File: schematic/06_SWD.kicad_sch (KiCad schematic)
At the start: 8 parts, among them J8 SWD_10pin, SW2 RESET

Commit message: Exclude JP1, JP2, TP1-TP20 from BOM (attrs only, sch+pcb)
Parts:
- TP10, TP7, TP8, TP9: now left out of the parts list
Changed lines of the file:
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@@
 		(unit 1)
 		(exclude_from_sim no)
-		(in_bom yes)
+		(in_bom no)
 		(on_board yes)
 		(dnp no)
@@
 		(unit 1)
 		(exclude_from_sim no)
-		(in_bom yes)
+		(in_bom no)
 		(on_board yes)
 		(dnp no)
@@
 		(unit 1)
 		(exclude_from_sim no)
-		(in_bom yes)
+		(in_bom no)
 		(on_board yes)
 		(dnp no)
@@
 		(unit 1)
 		(exclude_from_sim no)
-		(in_bom yes)
-		(on_board yes)
-		(dnp no)
+		(in_bom no)
+		(on_board yes)
+		(dnp no)

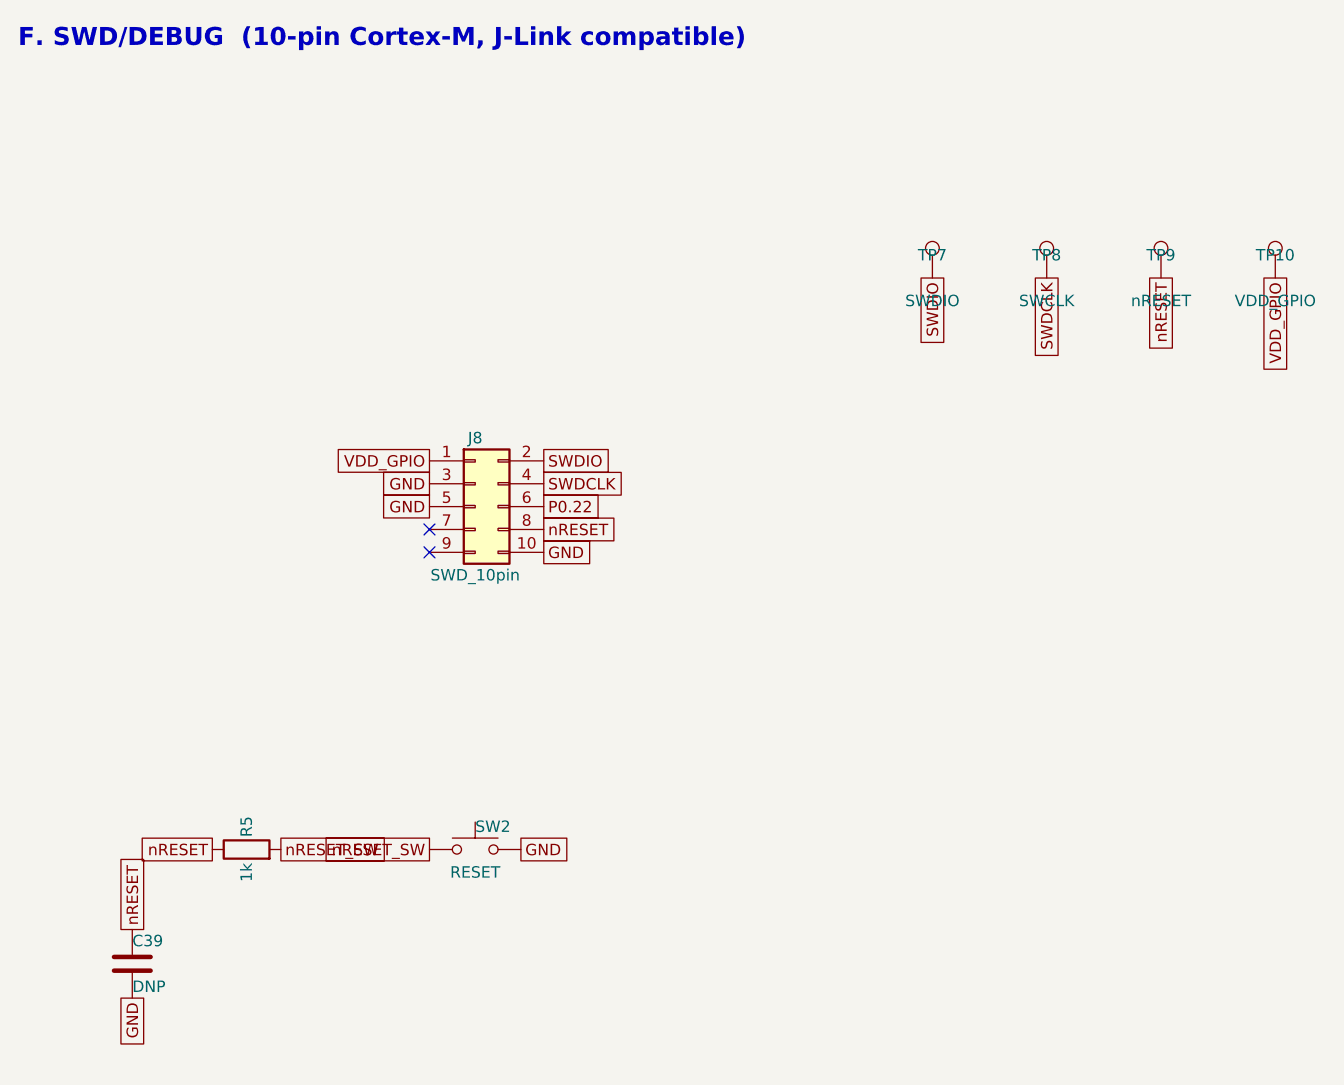
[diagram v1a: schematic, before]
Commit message: v2: simplify to UART modem module (J20 host header, LXC translators); remove J1, J3, J6, J9-J18, optional parts
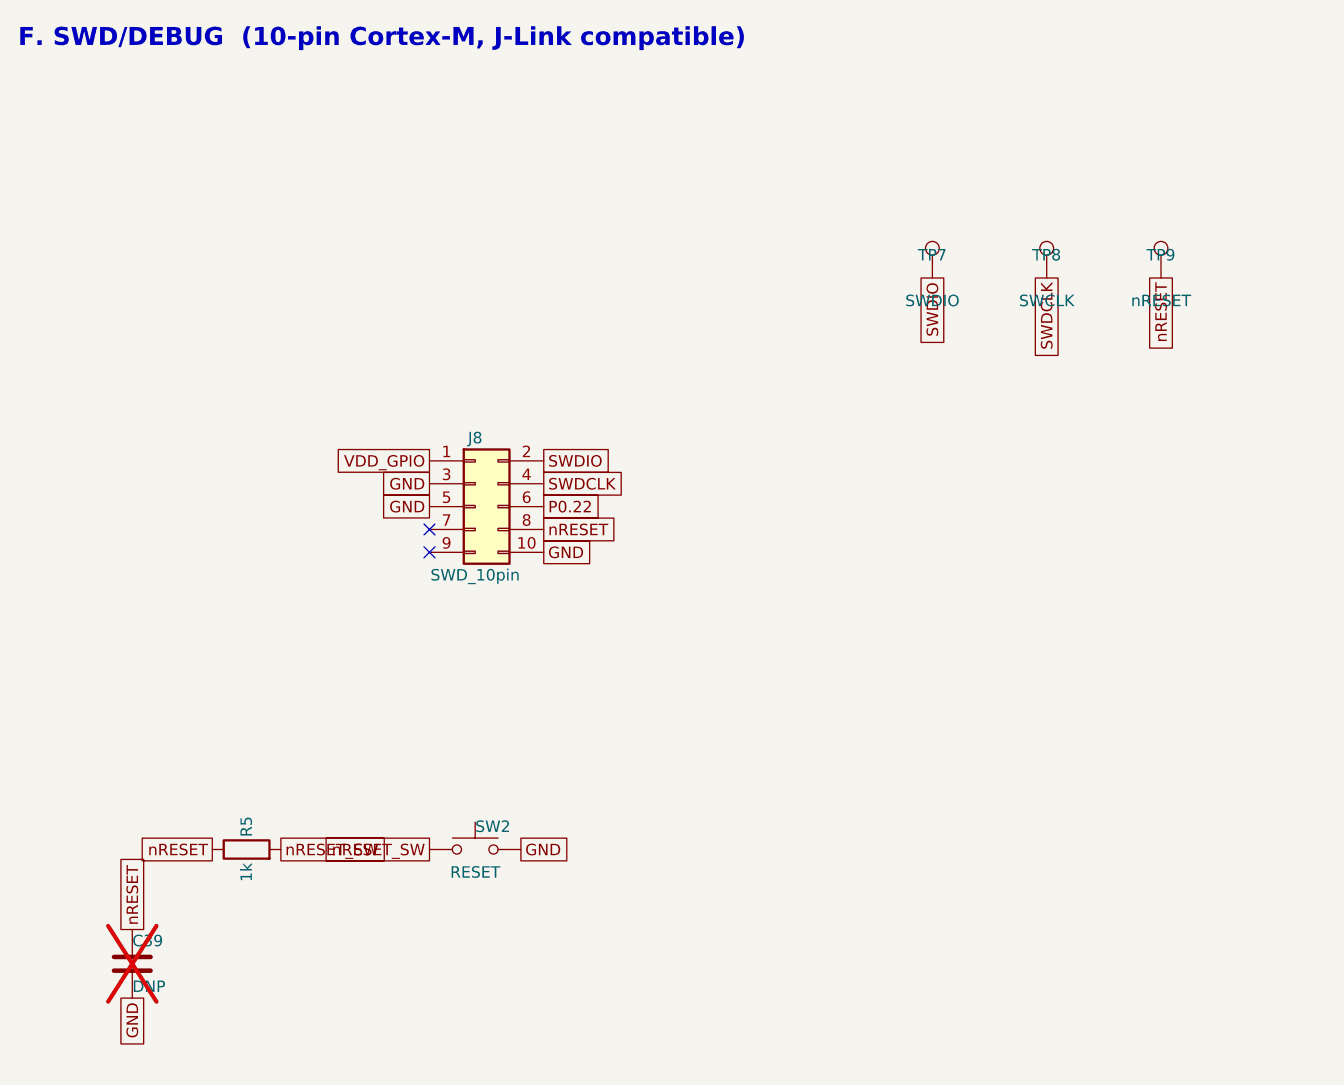
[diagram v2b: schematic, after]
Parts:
- removed TP10: VDD_GPIO, TestPoint:TestPoint_Pad_D1.5mm, symbol Connector:TestPoint
- C39: now not fitted; now left out of the parts list
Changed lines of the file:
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@@
 		(unit 1)
 		(exclude_from_sim no)
-		(in_bom yes)
+		(in_bom no)
 		(on_board yes)
-		(dnp no)
+		(dnp yes)
 		(property "Reference" "C39"
 			(at 38.1 111.76 0)
@@
 		)
 	)
-	(symbol
-		(lib_id "Connector:TestPoint")
-		(at 165.1 38.1 0)
-		(unit 1)
-		(exclude_from_sim no)
-		(in_bom no)
-		(on_board yes)
-		(dnp no)
-		(property "Reference" "TP10"
-			(at 165.1 35.56 0)
-			(show_name no)
-			(do_not_autoplace no)
-			(effects
-				(font
-					(size 1.27 1.27)
-				)
-			)
-		)
-		(property "Value" "VDD_GPIO"
-			(at 165.1 40.64 0)
-			(show_name no)
-			(do_not_autoplace no)
-			(effects
-				(font
-					(size 1.27 1.27)
-				)
-			)
-		)
-		(property "Footprint" "TestPoint:TestPoint_Pad_D1.5mm"
-			(at 170.18 38.1 0)
-			(hide yes)
-			(show_name no)
-			(do_not_autoplace no)
-			(effects
-				(font
-					(size 1.27 1.27)
-				)
-			)
-		)
-		(property "Datasheet" ""
-			(at 170.18 38.1 0)
-			(hide yes)
-			(show_name no)
-			(do_not_autoplace no)
-			(effects
-				(font
-					(size 1.27 1.27)
-				)
-			)
-		)
-		(property "Description" "test point"
-			(at 165.1 38.1 0)
-			(hide yes)
-			(show_name no)
-			(do_not_autoplace no)
-			(effects
-				(font
-					(size 1.27 1.27)
-				)
-			)
-		)
-		(pin "1"
-		)
-		(instances
-			(project "nRF9161-DEV-BOARD"
-				(path "/1d447b02-1bc4-4911-9534-6821deb40bd5"
-					(reference "TP10")
-					(unit 1)
-				)
-			 (path "/e1caf6a7-e2a0-4ff1-8424-4d92c0348b6b/b0fd138d-e5f5-4ca1-8a8b-2e0bf9d0b757" (reference "TP10") (unit 1)) (path "/e1caf6a7-e2a0-4ff1-8424-4d92c0348b6b/771cec44-91bf-49a5-8340-cd824d7c5092" (reference "TP10") (unit 1)))
-		)
-	)
 	(global_label "VDD_GPIO"
 		(at 71.12 58.42 180)
@@
 		(effects
 			(font
-				(size 1.27 1.27)
-			)
-			(justify right)
-		)
-	)
-	(global_label "VDD_GPIO"
-		(at 165.1 38.1 270)
-		(effects
-			(font

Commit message: v2 BOM: apply footprint-consistent MPNs + LCSC IDs, JLC BOM, audit reports (U4 footprint pending Layout)
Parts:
- J8: LCSC (none) -> C5155080; MPN (none) -> FTSH-105-01-L-DV-K; Manufacturer (none) -> Samtec
- R5: LCSC (none) -> C138165; MPN (none) -> RC0201FR-071KL; Manufacturer (none) -> Yageo
- SW2: LCSC (none) -> C778127; MPN (none) -> KXT331LHS; Manufacturer (none) -> C&K
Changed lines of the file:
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@@
+			)
+		)
+		(property "MPN" "FTSH-105-01-L-DV-K"
+			(at 76.2 63.5 0)
+			(hide yes)
+			(effects
+				(font
+					(size 1.27 1.27)
+				)
+			)
+		)
+		(property "LCSC" "C5155080"
+			(at 76.2 63.5 0)
+			(hide yes)
+			(effects
+				(font
+					(size 1.27 1.27)
+				)
+			)
+		)
+		(property "Manufacturer" "Samtec"
+			(at 76.2 63.5 0)
+			(hide yes)
+			(effects
+				(font
+					(size 1.27 1.27)
+				)
 			)
 		)
@@
 			)
 		)
+		(property "MPN" "RC0201FR-071KL"
+			(at 50.8 101.6 90)
+			(hide yes)
+			(effects
+				(font
+					(size 1.27 1.27)
+				)
+			)
+		)
+		(property "LCSC" "C138165"
+			(at 50.8 101.6 90)
+			(hide yes)
+			(effects
+				(font
+					(size 1.27 1.27)
+				)
+			)
+		)
+		(property "Manufacturer" "Yageo"
+			(at 50.8 101.6 90)
+			(hide yes)
+			(effects
+				(font
+					(size 1.27 1.27)
+				)
+			)
+		)
 		(pin "1"
 		)
@@
 			(effects
 				(font
+					(size 1.27 1.27)
+				)
+			)
+		)
+		(property "MPN" "KXT331LHS"
+			(at 76.2 101.6 0)
+			(hide yes)
+			(effects
+				(font
+					(size 1.27 1.27)
+				)
+			)
+		)
+		(property "LCSC" "C778127"
+			(at 76.2 101.6 0)
+			(hide yes)
+			(effects
+				(font
+					(size 1.27 1.27)
+				)
+			)
+		)
+		(property "Manufacturer" "C&K"
+			(at 76.2 101.6 0)
+			(hide yes)
+			(effects
+				(font
